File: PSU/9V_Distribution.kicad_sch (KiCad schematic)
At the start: 29 parts, among them J1 Screw_Terminal_2_P5.00mm, J2 Screw_Terminal_2_P5.00mm, J3 Screw_Terminal_2_P5.00mm, J4 Screw_Terminal_2_P5.00mm, J5 Screw_Terminal_2_P5.00mm, U1 P78A05-1000, U4 LM2596S-5

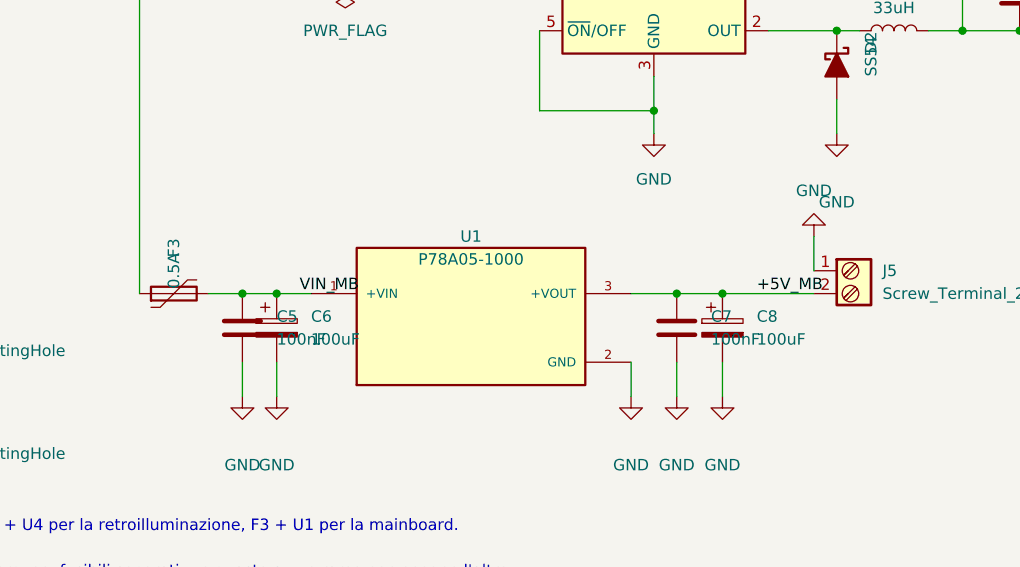
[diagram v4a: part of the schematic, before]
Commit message: Widen the mainboard to 270mm and place the supply selector
The 250mm board had no free rectangle left for the selector: counting
tracks and not just footprints, the largest gaps near the power section
were 14x12mm and 42x7mm, neither of which takes the screw terminal.

The board grows 20mm to the right, to (20,20)-(290,120). Nothing that
already existed moves except H3 and H7, which go from x 265 to x 285; the
other five mounting holes stay, so only two brass inserts move. The 100mm
depth is untouched. The ground zone follows the outline.

J13, C25, U8, C26, C27, R32, R33 and R34 go in the new strip as a column
at x 273..284, with 2.7 to 5mm between courtyards. J13 is rotated so its
wire entry faces the new right edge.

Net surgery: P1 pin 1 and R14 pin 1 change from +5V to VBUS, and the
thirteen tracks and one via that held P1.1 inside +5V are removed -- both
the path north to the y 105.72 spine and the bottom-layer branch that fed
the west group.

0 schematic parity issues. The 20 unconnected items are the new nets: the
GND ones clear on the first zone refill, the rest are for the autorouter.
Cutting P1.1 out of +5V splits that net into a west and an east island
which both now hang off U8 pin 7, and leaves the spine dangling at its
west end. The four silkscreen warnings and the three courtyard overlaps
were already there.

Co-Authored-By: Claude Opus 5 <noreply@anthropic.com>
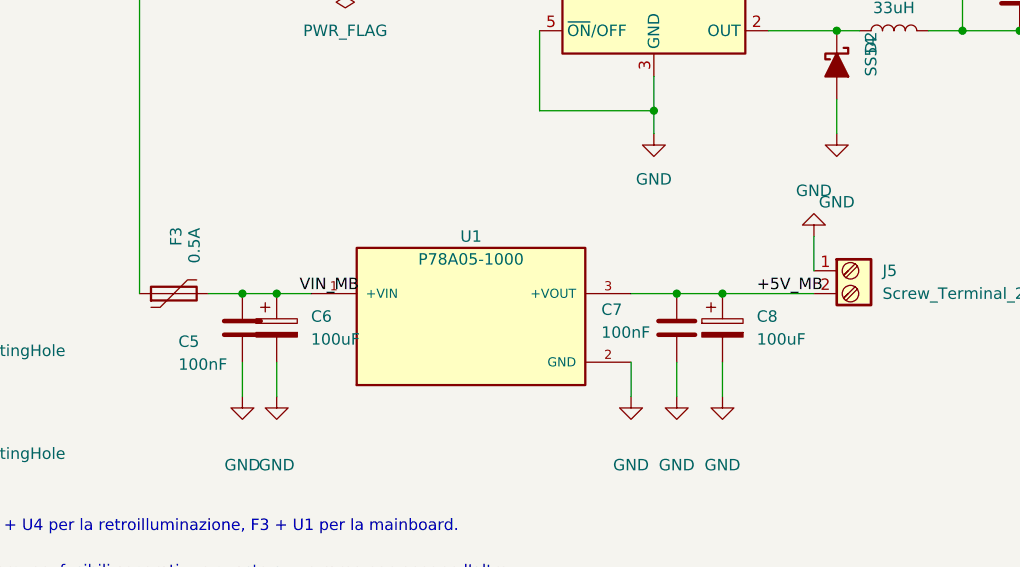
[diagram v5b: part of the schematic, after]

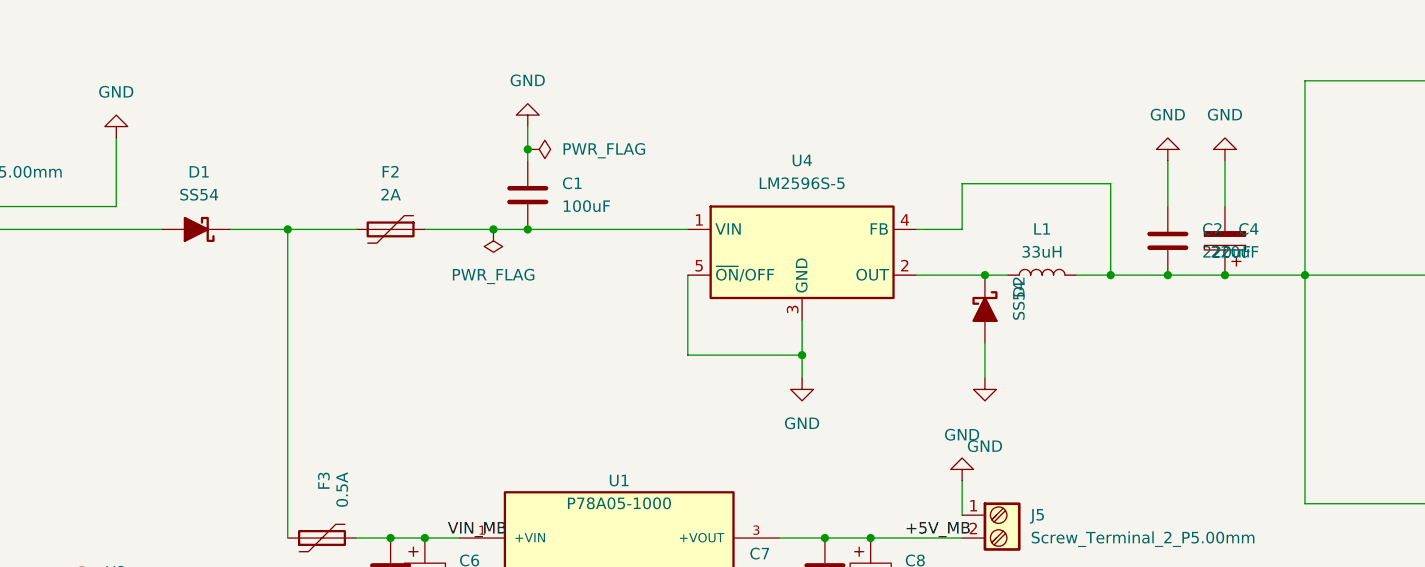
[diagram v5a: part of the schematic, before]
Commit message: Make the PSU buck section through-hole and give it room
D1, D2, C1 and C2 were SMD in among through-hole parts, for no better reason
than matching what the board already had. Two of the four conversions are
not about convenience:

  C1  sits across the 9V input and needs 25V of rating, which a 1206 MLCC of
      that capacitance does not come in. As an electrolytic the problem goes
      away instead of being documented.
  C2  is the buck's output capacitor and the LM2596 wants ESR there. As a
      ceramic it had none, which is why C4 exists; as an electrolytic it
      brings its own.

D1 and D2 become 1N5822 on the stock Device:D_Schottky symbol, which also
drops four missing-library warnings. Watch the polarity: the SS54 symbol has
pin 1 on the right and D_Schottky has it on the left, so both diodes are
rotated 180 to keep the cathode where it was -- the netlist confirms D1.2 on
the input, D2.1 on the switch node. D2 is mounted vertically on a 5.08mm
pitch, shorter than the SMC's 6.8mm, so the commutation loop tightened.

Side effect worth having: every ground pad in the buck section is now
through-hole and reaches both planes by itself, so four stitching vias and
their stubs are gone.

The whole section is re-placed and re-routed with room to work in, and the
P78A05 strip re-spaced to match. Nothing placed by hand is closer than 2mm
to its neighbour; the tightest pairs left are the original LED-and-resistor
pairs at 0.66mm.

0 unconnected items, 0 schematic parity issues. ERC is down from 15 to 11.
With the fill stripped there are no clearance, crossing, short or silkscreen
violations; 126 of the 138 the file reports are the stale pour and the other
12 are library links. Needs a refill in Pcbnew.

Co-Authored-By: Claude Opus 5 <noreply@anthropic.com>
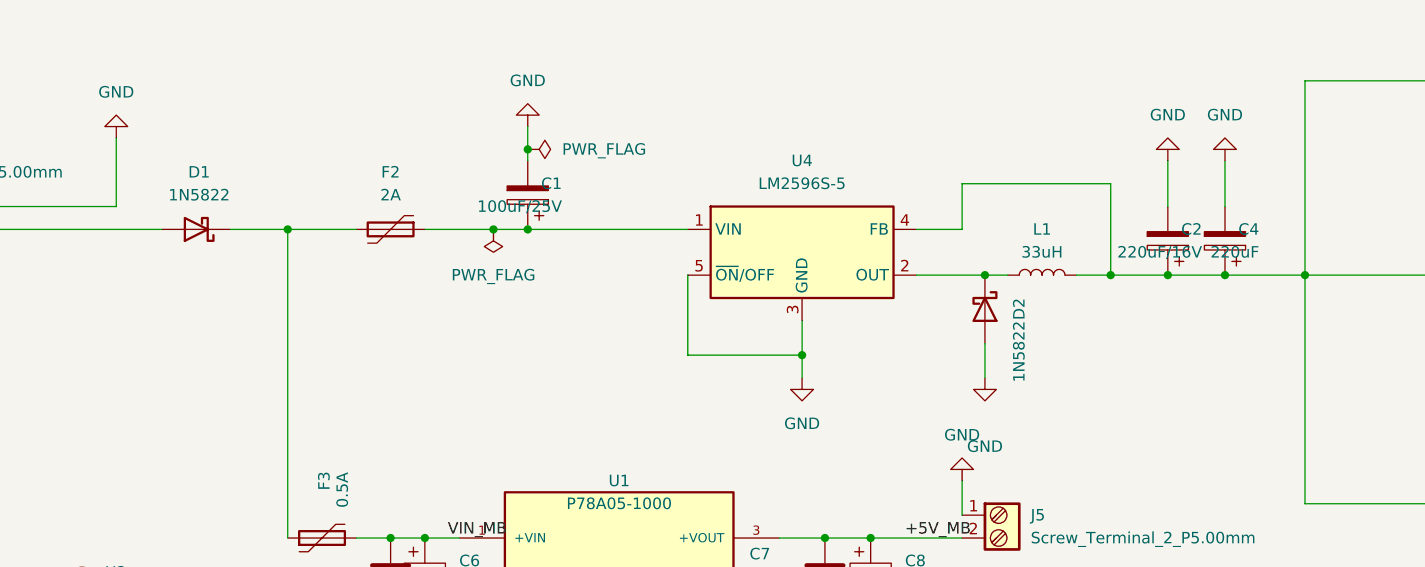
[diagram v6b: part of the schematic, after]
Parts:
- C1: value 100uF -> 100uF/25V; footprint Capacitor_SMD:C_1206_3216Metric_Pad1.33x1.80mm_HandSolder -> Capacitor_THT:CP_Radial_D6.3mm_P2.50mm; symbol Device:C -> Device:C_Polarized
- C2: value 220uF -> 220uF/16V; footprint Capacitor_SMD:C_1206_3216Metric_Pad1.33x1.80mm_HandSolder -> Capacitor_THT:CP_Radial_D6.3mm_P2.50mm; symbol Device:C -> Device:C_Polarized
- D1: value SS54 -> 1N5822; footprint PCM_Diode_SMD_AKL:D_SMC -> Diode_THT:D_DO-201AD_P12.70mm_Horizontal; symbol PCM_Diode_Schottky_AKL:SS54 -> Device:D_Schottky
- D2: value SS54 -> 1N5822; footprint PCM_Diode_SMD_AKL:D_SMC -> Diode_THT:D_DO-201AD_P5.08mm_Vertical_CathodeUp; symbol PCM_Diode_Schottky_AKL:SS54 -> Device:D_Schottky
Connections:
- net GND: now also C1.2, C2.2; no longer C1.1, C2.1
- net at F2.1, U4.1 (VIN): now also C1.1; no longer C1.2
- net at C4.1, J2.2, J3.2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: now also C2.1; no longer C2.2
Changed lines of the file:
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@@
 	)
 	(symbol
-		(lib_id "Device:C")
-		(at 102.87 72.39 0)
+		(lib_id "Device:C_Polarized")
+		(at 102.87 72.39 180)
 		(unit 1)
 		(body_style 1)
@@
 			)
 		)
-		(property "Value" "100uF"
+		(property "Value" "100uF/25V"
 			(at 106.68 73.6599 0)
 			(show_name no)
@@
 			)
 		)
-		(property "Footprint" "Capacitor_SMD:C_1206_3216Metric_Pad1.33x1.80mm_HandSolder"
+		(property "Footprint" "Capacitor_THT:CP_Radial_D6.3mm_P2.50mm"
 			(at 103.8352 76.2 0)
 			(hide yes)
@@
 			)
 		)
-		(property "Description" "Unpolarized capacitor"
+		(property "Description" "Polarized capacitor"
 			(at 102.87 72.39 0)
 			(hide yes)
@@
 	)
 	(symbol
-		(lib_id "PCM_Diode_Schottky_AKL:SS54")
-		(at 153.67 85.09 90)
+		(lib_id "Device:D_Schottky")
+		(at 153.67 85.09 270)
 		(unit 1)
 		(body_style 1)
@@
 			)
 		)
-		(property "Value" "SS54"
+		(property "Value" "1N5822"
 			(at 157.48 86.3599 0)
 			(show_name no)
@@
 			)
 		)
-		(property "Footprint" "PCM_Diode_SMD_AKL:D_SMC"
+		(property "Footprint" "Diode_THT:D_DO-201AD_P5.08mm_Vertical_CathodeUp"
 			(at 153.67 85.09 0)
 			(hide yes)
@@
 			)
 		)
-		(property "Datasheet" "https://www.laro.com.pl/pdf/ss56.pdf"
+		(property "Datasheet" "https://www.diodes.com/assets/Datasheets/ds23001.pdf"
 			(at 153.67 85.09 0)
 			(hide yes)
@@
 			)
 		)
-		(property "Description" "SMC Schottky diode, 40V, 5A, Alternate KiCAD Library"
+		(property "Description" "40V 3A Schottky Barrier Rectifier Diode, DO-201AD"
 			(at 153.67 85.09 0)
 			(hide yes)
@@
 	)
 	(symbol
-		(lib_id "PCM_Diode_Schottky_AKL:SS54")
-		(at 66.04 76.2 0)
+		(lib_id "Device:D_Schottky")
+		(at 66.04 76.2 180)
 		(unit 1)
 		(body_style 1)
@@
 			)
 		)
-		(property "Value" "SS54"
+		(property "Value" "1N5822"
 			(at 66.3575 72.39 0)
 			(show_name no)
@@
 			)
 		)
-		(property "Footprint" "PCM_Diode_SMD_AKL:D_SMC"
+		(property "Footprint" "Diode_THT:D_DO-201AD_P12.70mm_Horizontal"
 			(at 66.04 76.2 0)
 			(hide yes)
@@
 			)
 		)
-		(property "Datasheet" "https://www.laro.com.pl/pdf/ss56.pdf"
+		(property "Datasheet" "https://www.diodes.com/assets/Datasheets/ds23001.pdf"
 			(at 66.04 76.2 0)
 			(hide yes)
@@
 			)
 		)
-		(property "Description" "SMC Schottky diode, 40V, 5A, Alternate KiCAD Library"
+		(property "Description" "40V 3A Schottky Barrier Rectifier Diode, DO-201AD"
 			(at 66.04 76.2 0)
 			(hide yes)
@@
 	)
 	(symbol
-		(lib_id "Device:C")
-		(at 173.99 77.47 0)
+		(lib_id "Device:C_Polarized")
+		(at 173.99 77.47 180)
 		(unit 1)
 		(body_style 1)
@@
 			)
 		)
-		(property "Value" "220uF"
+		(property "Value" "220uF/16V"
 			(at 177.8 78.7399 0)
 			(show_name no)
@@
 			)
 		)
-		(property "Footprint" "Capacitor_SMD:C_1206_3216Metric_Pad1.33x1.80mm_HandSolder"
+		(property "Footprint" "Capacitor_THT:CP_Radial_D6.3mm_P2.50mm"
 			(at 174.9552 81.28 0)
 			(hide yes)
@@
 			)
 		)
-		(property "Description" "Unpolarized capacitor"
+		(property "Description" "Polarized capacitor"
 			(at 173.99 77.47 0)
 			(hide yes)

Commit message: Give the 9 V rail a name
La classe di rete da 1.0 mm cercava una rete chiamata +9V che non esisteva:
il ramo dei 9 V non aveva nome e si chiamava Net-(D1-A), Net-(D1-K),
Net-(U4-VIN). Quindi la classe non prendeva niente, e una pista nuova su
quel ramo sarebbe uscita da 0.2 mm, la larghezza del Default. Il ramo della
mainboard un nome ce l'aveva gia', VIN_MB; questo no.

Tre etichette sui fili che c'erano gia', nello stile delle altre del foglio:

  9V_IN   J1 -> anodo di D1, prima della protezione contro l'inversione
  9V      catodo di D1 -> F2 e F3, il tronco protetto
  9V_BL   F2 -> VIN del buck, il ramo del backlighting

Le etichette locali prendono il prefisso del foglio, quindi le reti si
chiamano /9V_IN, /9V, /9V_BL e il pattern della classe diventa /9V*.

Nessun rame spostato: cambiano solo le stringhe del nome rete su pad e
piste. I gerber escono identici, i nomi non stanno su nessun livello di
fabbricazione.

Netlist verificata: /9V_IN = D1.2 J1.1, /9V = D1.1 F2.2 F3.1,
/9V_BL = C1.1 F2.1 U4.1. ERC identico a prima, DRC 3 violazioni di
libreria, 0 scollegamenti, 0 parita'.

Co-Authored-By: Claude Opus 5 <noreply@anthropic.com>
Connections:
- net 9V_BL: now reaches C1.1, F2.1, U4.1 (VIN)
- net 9V: now reaches D1.1 (K), F2.2, F3.1
- net 9V_IN: now reaches D1.2 (A), J1.1
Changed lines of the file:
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@@
 	)
 	(embedded_fonts no)
+	(label "9V_IN"
+		(at 50.8 76.2 0)
+		(effects
+			(font
+				(size 1.27 1.27)
+			)
+			(justify left bottom)
+		)
+	)
+	(label "9V"
+		(at 72.39 76.2 0)
+		(effects
+			(font
+				(size 1.27 1.27)
+			)
+			(justify left bottom)
+		)
+	)
+	(label "9V_BL"
+		(at 110.49 76.2 0)
+		(effects
+			(font
+				(size 1.27 1.27)
+			)
+			(justify left bottom)
+		)
+	)
 )

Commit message: Drop the PCM symbols the boards did not need
Gli ERC che restavano erano quasi tutti simboli presi da librerie PCM che
bisogna installare a parte. Dove KiCad ha il suo equivalente con gli stessi
pin, tanto vale usarlo e non chiedere niente a chi apre il repository.

PSU: i cinque morsetti passano da PCM_SL_Screw_Terminal a
Connector:Screw_Terminal_01x02. Il simbolo di libreria ha i pin 1.27 mm piu'
in fuori e 1.27 piu' in basso, quindi ogni simbolo e' stato spostato di
altrettanto, ruotato come il componente, e i fili che c'erano restano
attaccati dove stavano. Netlist verificata pin per pin. ERC da 5 a 0.

Cambiare quel simbolo ha pero' rinominato da solo il nodo dei 5 V del
backlighting, che non aveva nome e si chiamava a seconda di quale pin
capitava primo: Net-(LED1-A) e' diventato Net-(J2-Pin_2) e la parita' e'
saltata su dieci pad. Invece di inseguire il nome automatico gliene ho dato
uno vero, 5V_BL, come al ramo dei 9 V.

Dimmer e i due Korry: riallineate alla libreria le definizioni incorporate
di IRLIZ44N e LED. Prima di sostituirle ho confrontato i pin: identici, se
no i fili sarebbero rimasti attaccati al vuoto.

Restano due avvisi, uno sul dimmer e uno sul Korry grande, e li lascio
apposta:
 - il NE555 di Digi-Key ha una disposizione dei pin diversa da quella dei
   555 in libreria, quindi lo scambio vorrebbe rifare tutti i collegamenti;
 - lo switch tattile di Digi-Key numera i pin 1-2 da una parte e 3-4
   dall'altra, Switch:SW_Push_Dual li numera 1-3 e 2-4. Le posizioni
   coincidono, la numerazione no: scambiarlo cambierebbe quali pioli sono
   in corto dentro al pulsante.
Tutti e due i simboli sono incorporati nei file e sono corretti; installare
la libreria Digi-Key li fa tacere.

Stato: sei schede, quattro pulite su tutto. Dimmer 1 ERC e 1 DRC, Korry
grande 1 ERC. Tutte a 0 scollegamenti e 0 parita'.

Co-Authored-By: Claude Opus 5 <noreply@anthropic.com>
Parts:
- J1, J2, J3, J4, J5: symbol PCM_SL_Screw_Terminal:Screw_Terminal_2_P5.00mm -> Connector:Screw_Terminal_01x02
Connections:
- net 5V_BL: now reaches C2.1, C4.1, J2.2 (Pin_2), J3.2 (Pin_2), J4.2 (Pin_2), L1.2, LED1.2 (A), LED2.2 (A), LED3.2 (A), U4.4 (FB)
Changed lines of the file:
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@@
 	)
 	(symbol
-		(lib_id "PCM_SL_Screw_Terminal:Screw_Terminal_2_P5.00mm")
-		(at 154.94 109.22 0)
+		(lib_id "Connector:Screw_Terminal_01x02")
+		(at 156.21 107.95 0)
 		(unit 1)
 		(body_style 1)
@@
 	)
 	(symbol
-		(lib_id "PCM_SL_Screw_Terminal:Screw_Terminal_2_P5.00mm")
-		(at 234.95 58.42 0)
+		(lib_id "Connector:Screw_Terminal_01x02")
+		(at 236.22 57.15 0)
 		(unit 1)
 		(body_style 1)
@@
 	)
 	(symbol
-		(lib_id "PCM_SL_Screw_Terminal:Screw_Terminal_2_P5.00mm")
-		(at 234.95 105.41 0)
+		(lib_id "Connector:Screw_Terminal_01x02")
+		(at 236.22 104.14 0)
 		(unit 1)
 		(body_style 1)
@@
 	)
 	(symbol
-		(lib_id "PCM_SL_Screw_Terminal:Screw_Terminal_2_P5.00mm")
-		(at 39.37 74.93 180)
+		(lib_id "Connector:Screw_Terminal_01x02")
+		(at 38.1 76.2 180)
 		(unit 1)
 		(body_style 1)
@@
 	)
 	(symbol
-		(lib_id "PCM_SL_Screw_Terminal:Screw_Terminal_2_P5.00mm")
-		(at 234.95 80.01 0)
+		(lib_id "Connector:Screw_Terminal_01x02")
+		(at 236.22 78.74 0)
 		(unit 1)
 		(body_style 1)
@@
 		(effects
 			(font
+				(size 1.27 1.27)
+			)
+			(justify left bottom)
+		)
+	)
+	(label "5V_BL"
+		(at 215.9 59.69 0)
+		(effects
+			(font
